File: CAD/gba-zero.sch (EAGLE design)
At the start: 17 parts, among them IC5 APX803, Q2 BSS138

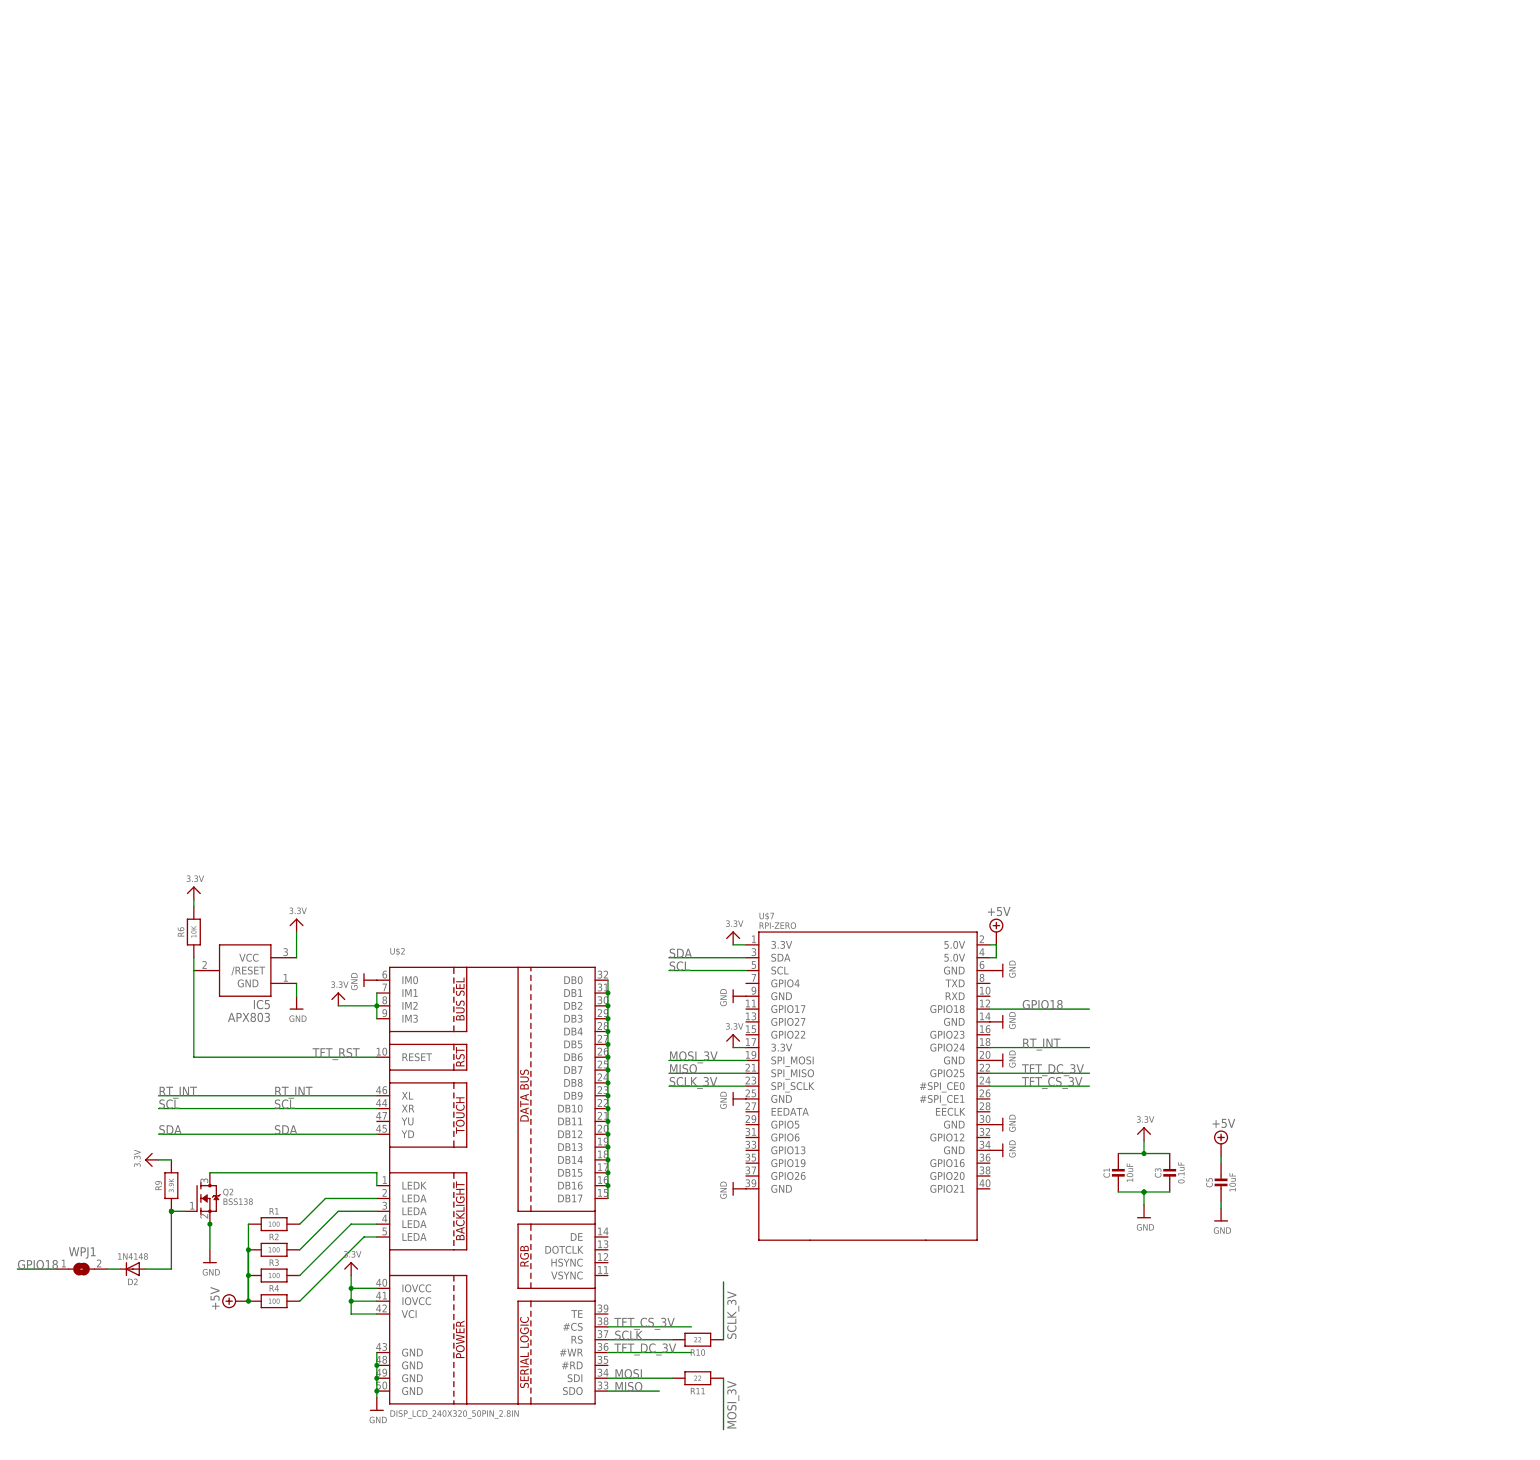
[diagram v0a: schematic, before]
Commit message: Parts & Schematic almost done, except AB buttons
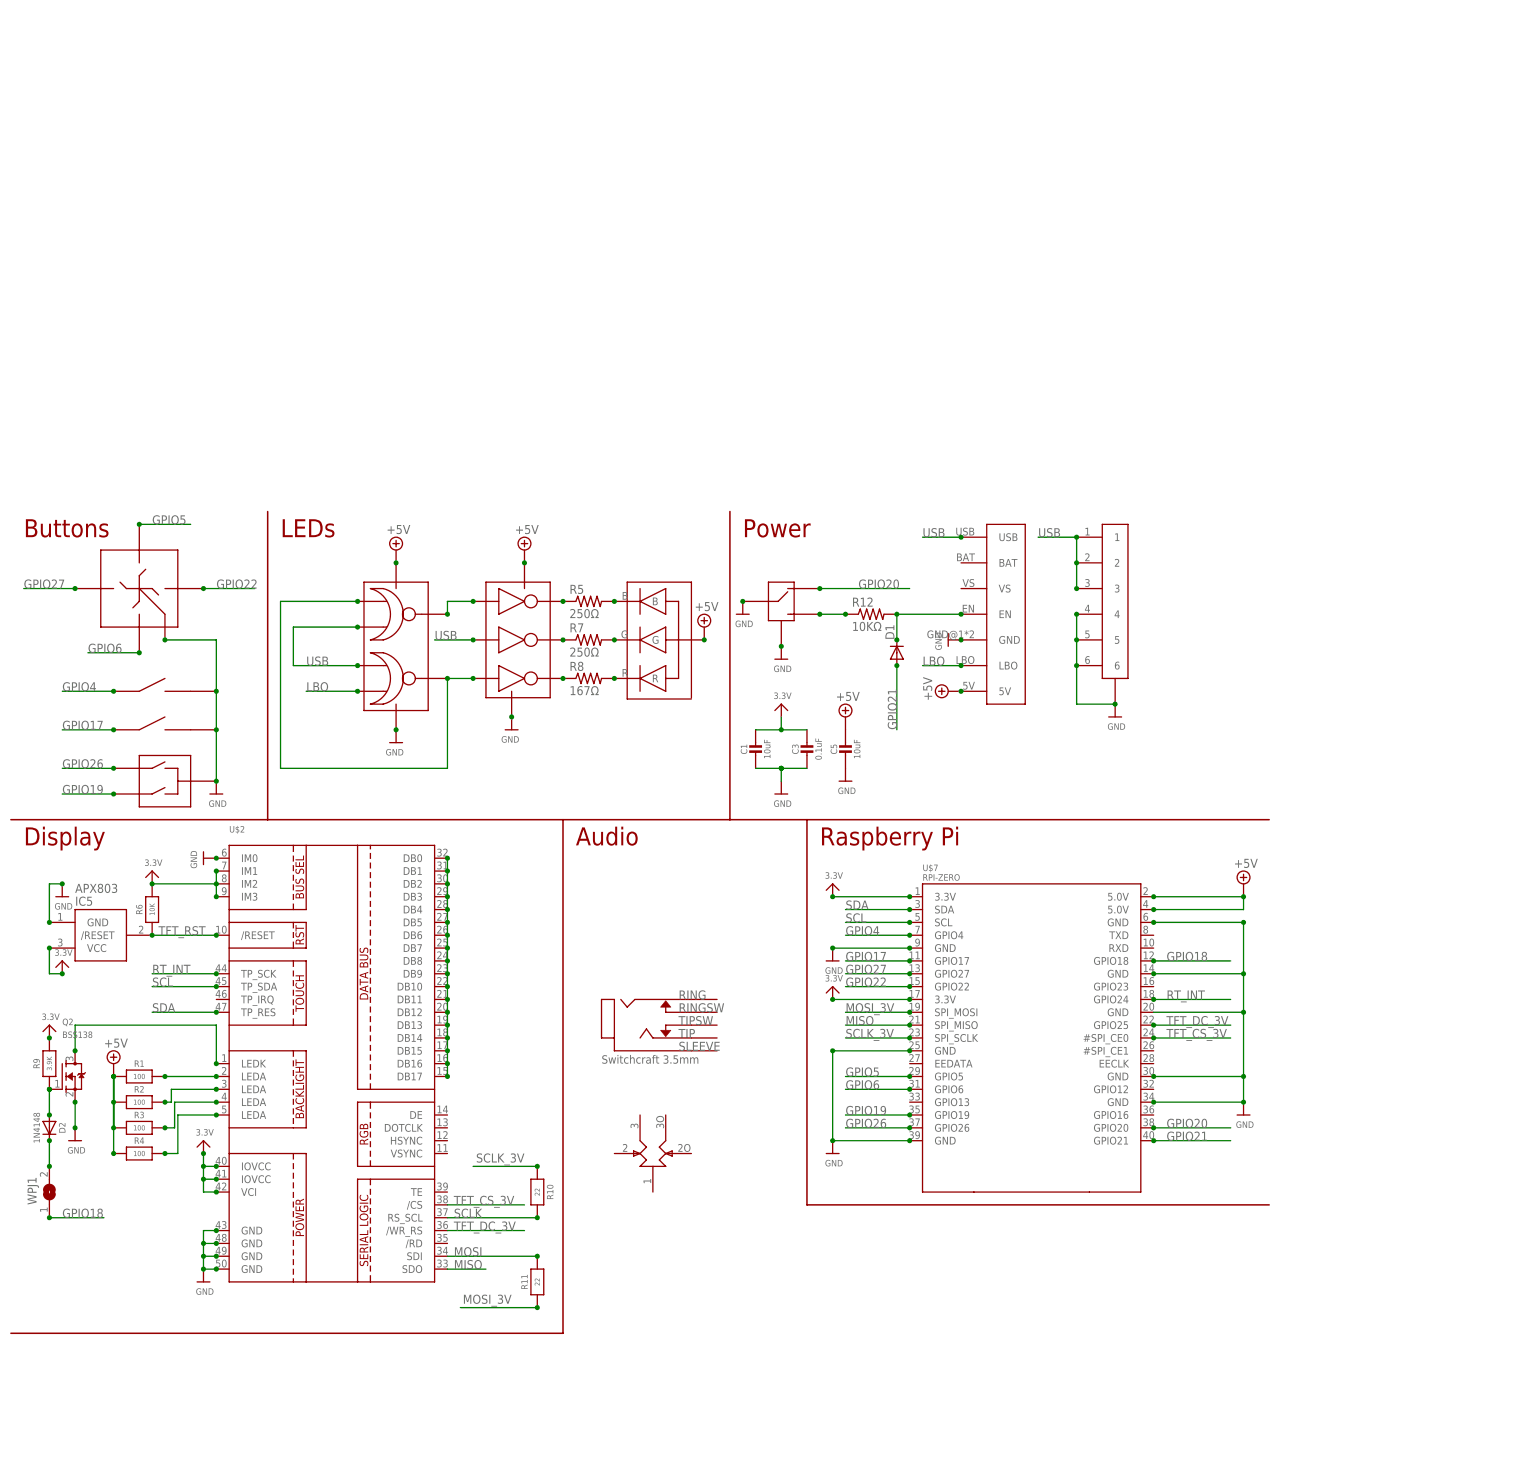
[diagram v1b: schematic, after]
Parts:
- added D1: (no value), diode:DIODE-D-5
- added R12: 10KΩ, resistor:R-US_R0603
- added R5, R7: 250Ω, resistor:R-US_R0603
- added R8: 167Ω, resistor:R-US_R0603
- added U$10: LINK_CONNECTOR, gba-zero-parts:LINK_CONNECTOR
- added U$11: PWR_SWITCH, gba-zero-parts:PWR_SWITCH
- added U$12: POWERBOOST-1000C, gba-zero-parts:POWERBOOST-1000C
- added U$15: RK10J12E0A0A, gba-zero-parts:RK10J12E0A0A
- added U$16, U$17: SHOULDER_BUTTON, gba-zero-parts:SHOULDER_BUTTON
- added U$18: START_SELECT_BUTTON, gba-zero-parts:START_SELECT_BUTTON
- added U$22: SWTCHCRFT_3.5JACK5-JACK-SMD, gba-zero-parts:SWTCHCRFT_3.5JACK5-JACK-SMD
- added U$3: D-PAD, gba-zero-parts:D-PAD
- added U$42: 74LVC2G02, gba-zero-parts:74LVC2G02
- added U$43: 74LVC3G04, gba-zero-parts:74LVC3G04
- added U$44: LTST-C19HE1WT, gba-zero-parts:LTST-C19HE1WT
- U$2: value DISP_LCD_240X320_50PIN_2.8IN -> (none); device microbuilder:DISP_LCD_240X320_50PIN_2.8IN -> gba-zero-parts:DISP_LCD_CTP28_SAMPLE
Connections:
- new net GPIO17: U$17.1, U$7.GPIO17
- new net GPIO19: U$18.SEL, U$7.GPIO19
- new net GPIO20: U$11.L, U$7.GPIO20
- new net GPIO21: D1.A, U$7.GPIO21
- new net GPIO22: U$3.RIGHT, U$7.GPIO22
- new net GPIO26: U$18.STR, U$7.GPIO26
- new net GPIO27: U$3.LEFT, U$7.GPIO27
- new net GPIO4: U$16.1, U$7.GPIO4
- new net GPIO5: U$3.UP, U$7.GPIO5
- new net GPIO6: U$3.DOWN, U$7.GPIO6
- new net LBO: U$12.LBO, U$42.2B
- new net N$11: R8.1, U$43.3Y
- new net N$12: R5.2, U$44.B
- new net N$13: R7.2, U$44.G
- new net N$14: R8.2, U$44.R
- new net N$15: U$42.1Y, U$43.1A
- new net N$16: U$42.1A, U$42.2Y, U$43.3A
- new net N$17: R12.1, U$11.R
- new net N$18: D1.C, R12.2, U$12.EN
- new net N$5: R5.1, U$43.1Y
- new net N$8: R7.1, U$43.2Y
- new net USB: U$10.1, U$10.2, U$10.3, U$12.USB, U$42.1B, U$42.2A, U$43.2A
- net +5V: now also U$12.5V, U$42.VCC, U$43.VCC, U$44.VCC
- net GND: now also U$10.4, U$10.5, U$10.6, U$10.GND, U$11.C, U$11.GND, U$12.GND, U$16.2, U$17.2, U$18.GND, U$3.GND, U$42.GND, U$43.GND
- net RT_INT: now also U$2.TP_SCK; no longer U$2.XL
- net SCL: now also U$2.TP_SDA; no longer U$2.XR
- net SCLK: now also U$2.RS_SCL; no longer U$2.RS
- net SDA: now also U$2.TP_RES; no longer U$2.YD
- net TFT_CS_3V: now also U$2./CS; no longer U$2.#CS
- net TFT_DC_3V: now also U$2./WR_RS; no longer U$2.#WR
- net TFT_RST: now also U$2./RESET; no longer U$2.RESET
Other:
- note added: "Audio"
- note added: "Buttons"
- note added: "Display"
- note added: "LEDs"
- note added: "Power"
- note added: "Raspberry Pi"
- moved on the sheet: C1, C3, C5, D2, IC5, Q2, R1, R10, R11, R2, R3, R4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

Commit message: Added AB_BUTTON part to library & schematic
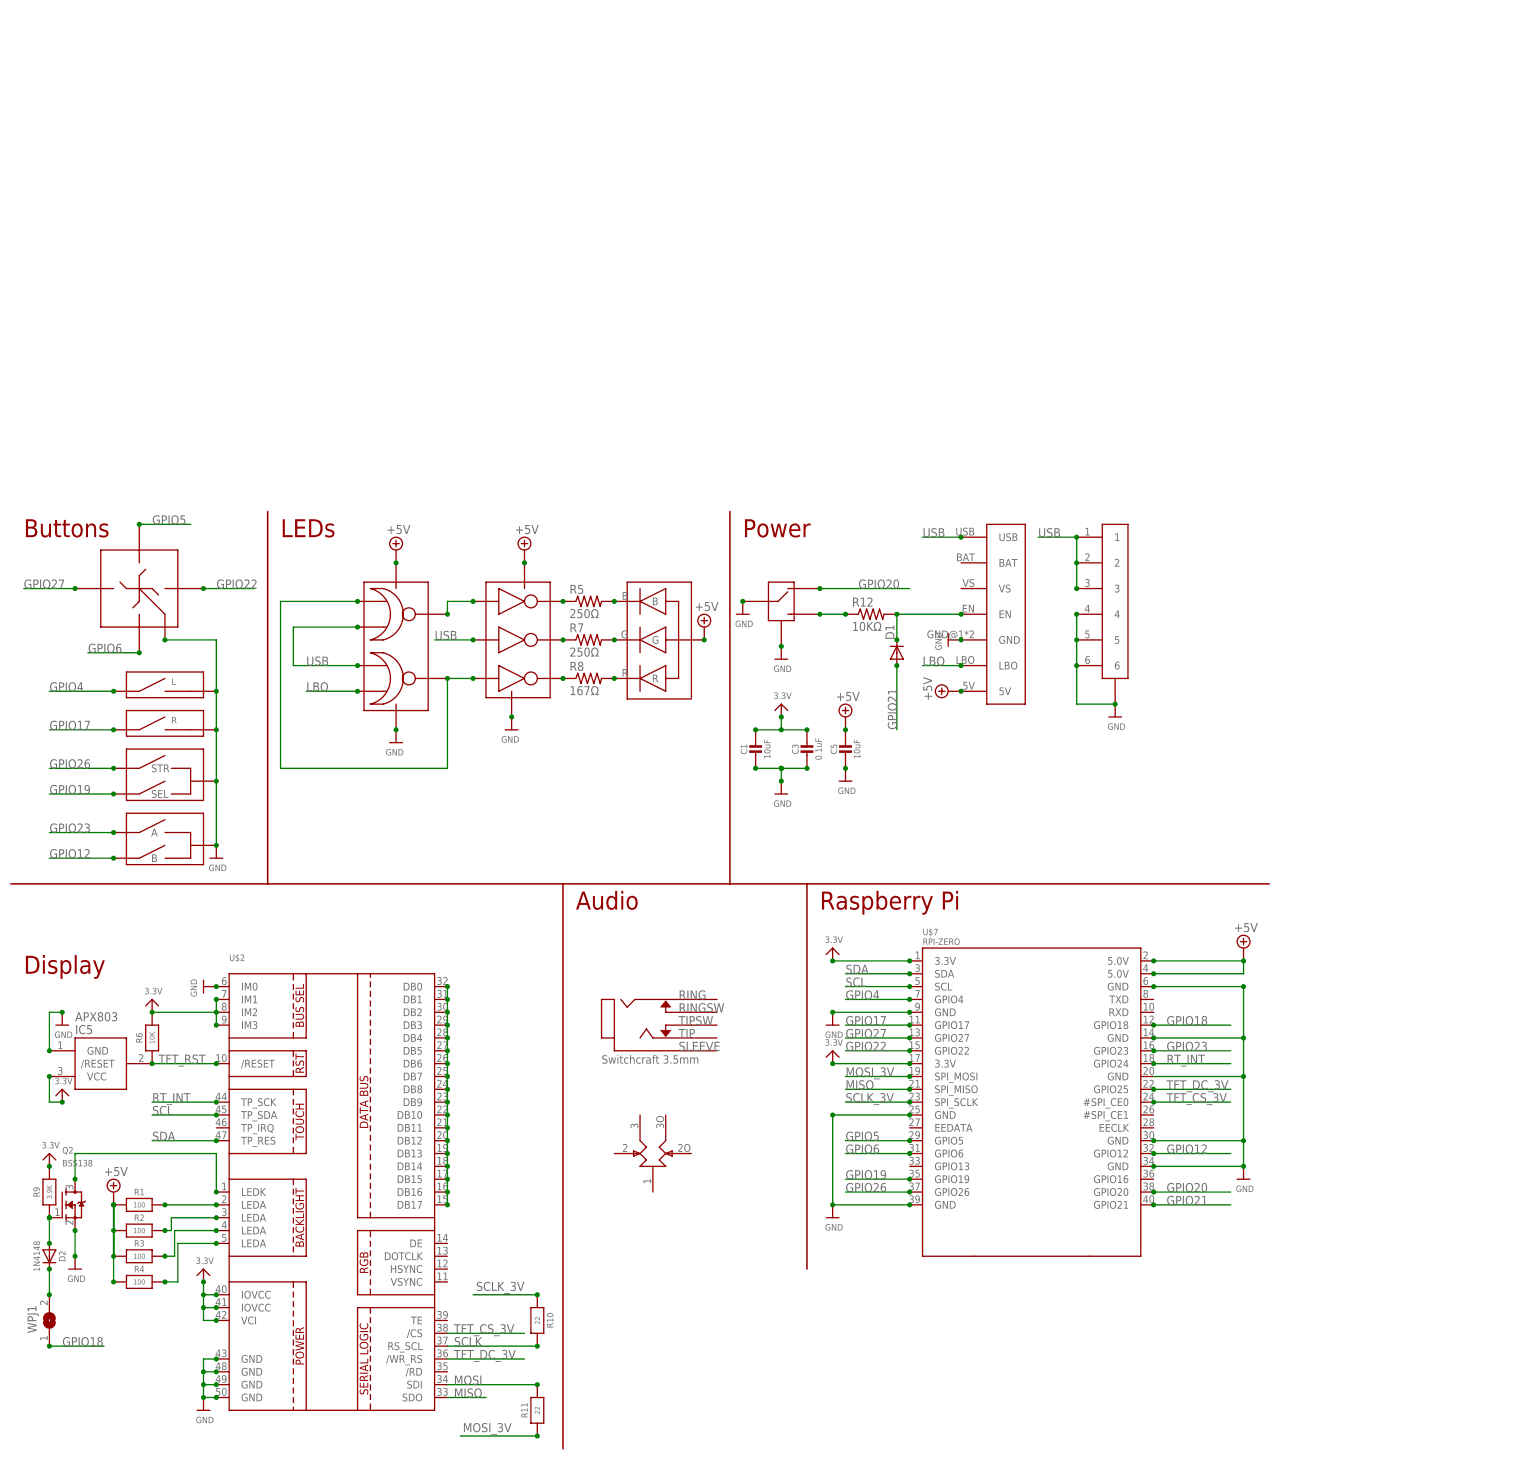
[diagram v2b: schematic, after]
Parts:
- added U$20: AB_BUTTON, gba-zero-parts:AB_BUTTON
- renumbered U$16 to L, U$17 to R
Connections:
- new net 5.0V: C5.1, R1.1, R2.1, R3.1, R4.1, U$12.5V, U$42.VCC, U$43.VCC, U$44.VCC
- new net GPIO12: U$20.B, U$7.GPIO12
- new net GPIO23: U$20.A, U$7.GPIO23
- net +5V: no longer C5.1, R1.1, R2.1, R3.1, R4.1, U$12.5V, U$42.VCC, U$43.VCC, U$44.VCC
- net GND: now also U$20.GND
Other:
- moved on the sheet: D2, IC5, Q2, R1, R10, R11, R2, R3, R4, R6, R9, U$2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
